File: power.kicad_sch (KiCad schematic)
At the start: 63 parts, among them U605 TPS566231P, U606 TPS566231P, U607 TPS566231P, U608 TPS566231P

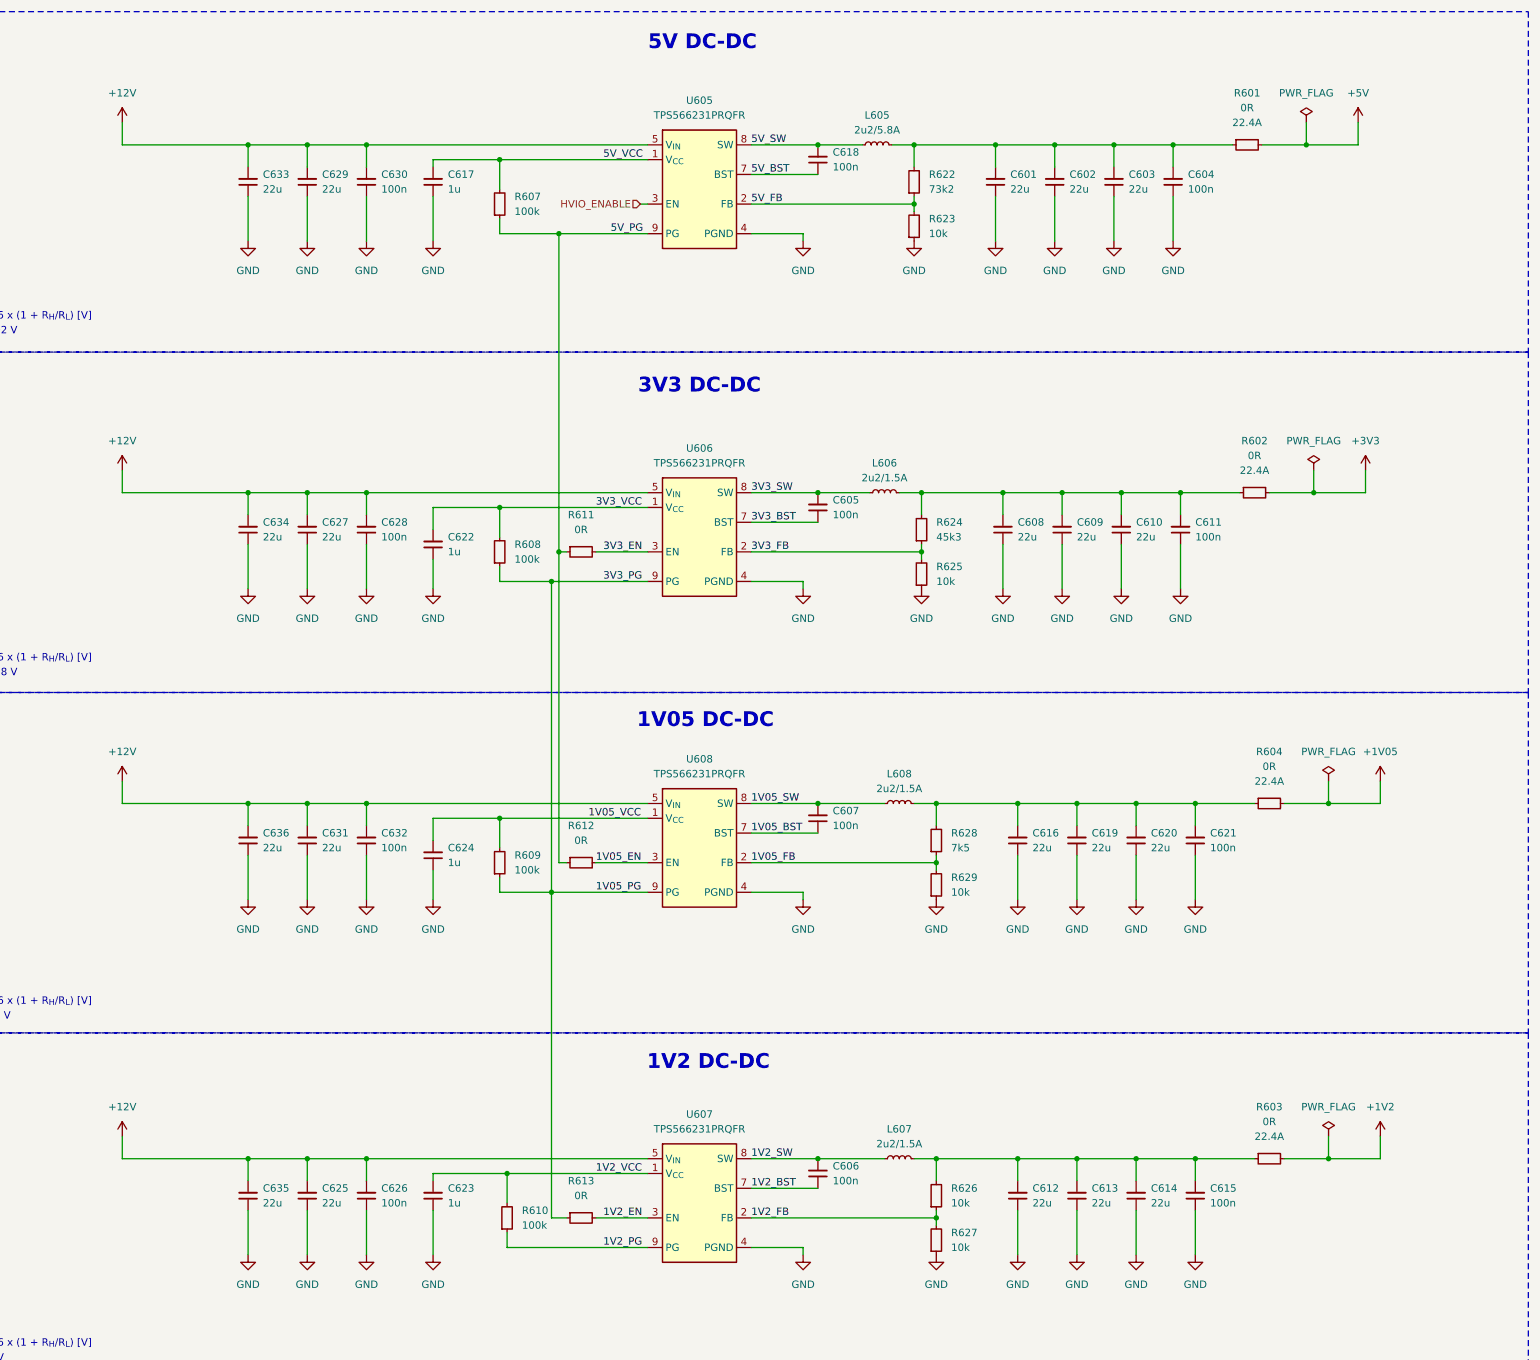
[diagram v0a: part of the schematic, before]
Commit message: [#99974] Import DC-SCM ports on root schematic, start connecting them to other blocks
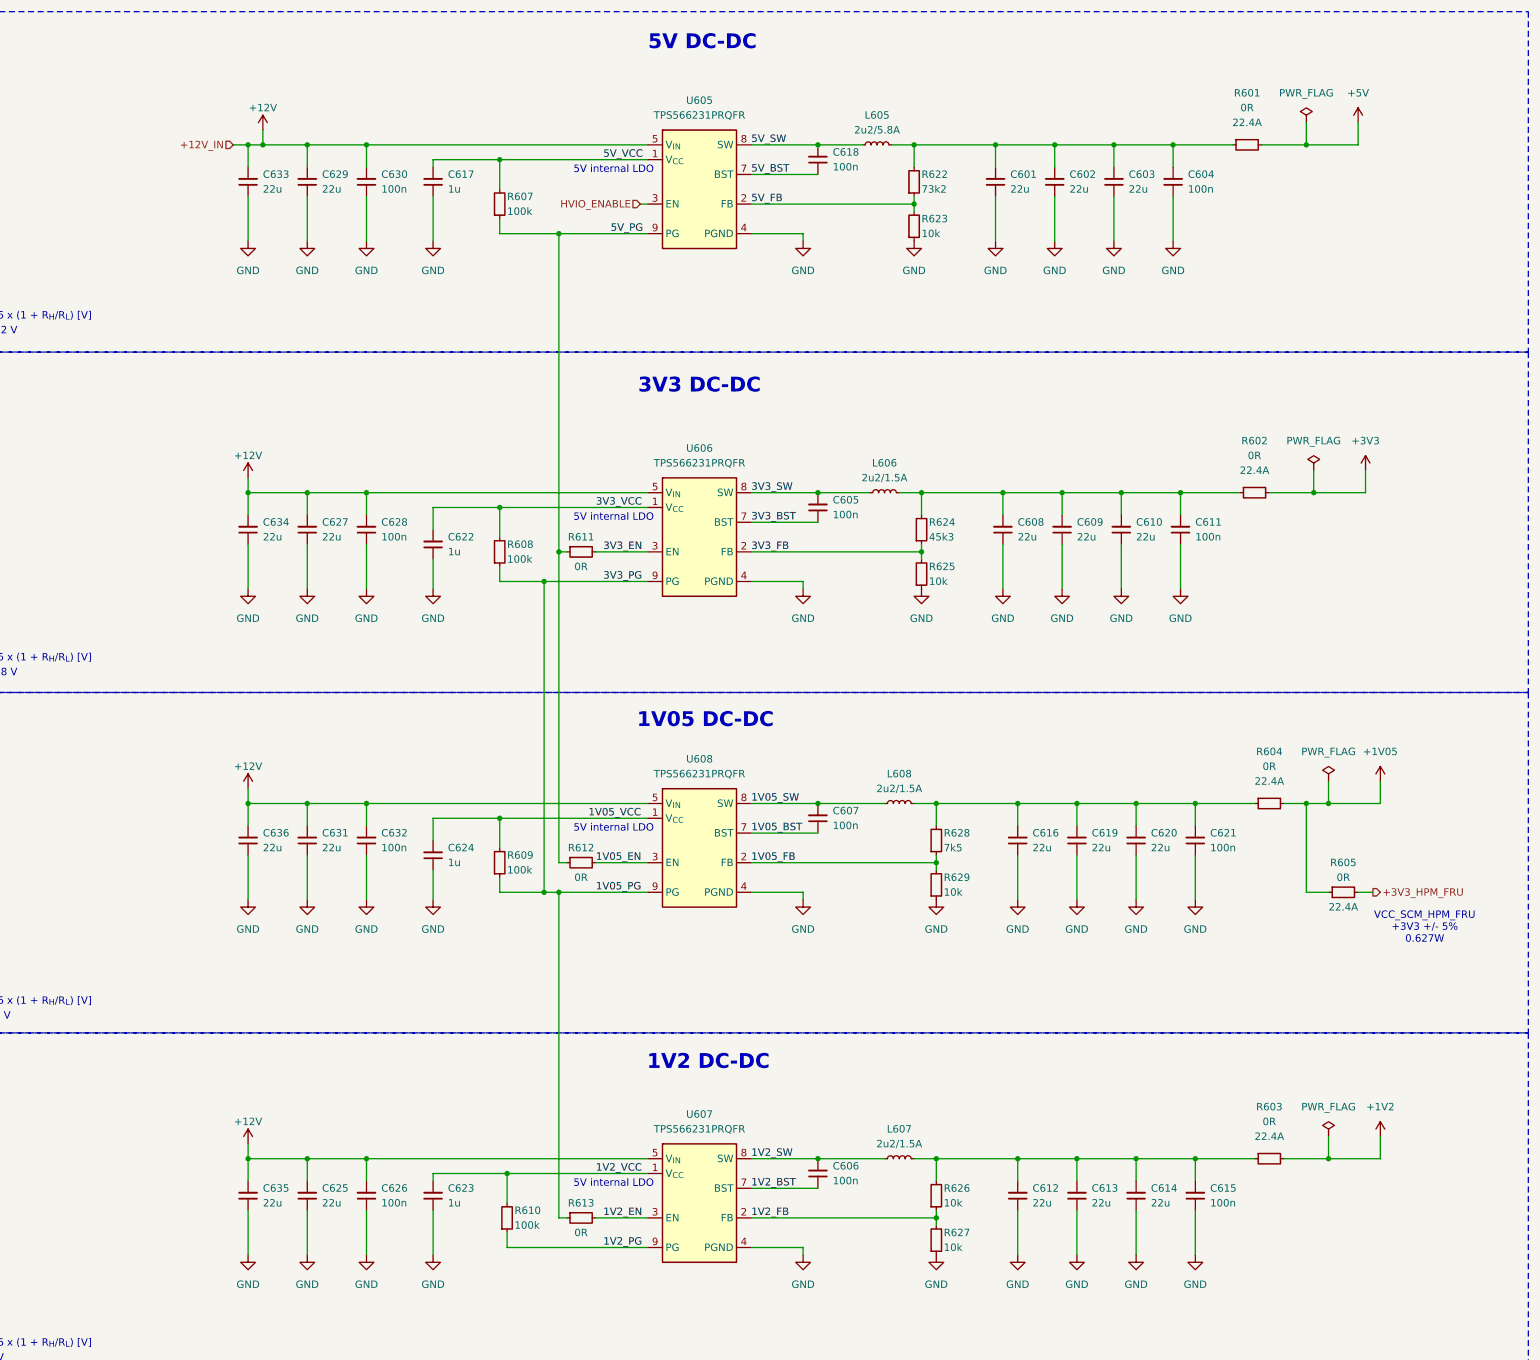
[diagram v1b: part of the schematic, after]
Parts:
- added R605: R_0R_22.4A_0603, antmicro-footprints:R_0603_1608Metric, symbol antmicroResistors0603:R_0R_22.4A_0603
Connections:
- net +1V05: now also R605.1
- new net +3V3_HPM_FRU: R605.2
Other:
- note added: "5V internal LDO"
- note added: "VCC_SCM_HPM_FRU +3V3 +/- 5% 0.627W"

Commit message: [#99649] Fix HS connector rule area, add DP AUX, HPD and CONFIG pins to DP bus, connect most signals on root schematic
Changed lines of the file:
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@@
 		(company "Altera")
-	)
-	(rectangle
-		(start 72.39 193.04)
-		(end 347.98 251.46)
-		(stroke
-			(width 0)
-			(type dash)
-			(color 7 57 255 1)
-		)
-		(fill
-			(type none)
-		)
-	)
-	(rectangle
-		(start 72.39 17.78)
-		(end 347.98 76.2)
-		(stroke
-			(width 0)
-			(type dash)
-			(color 7 57 255 1)
-		)
-		(fill
-			(type none)
-		)
-	)
-	(rectangle
-		(start 72.39 134.62)
-		(end 347.98 193.04)
-		(stroke
-			(width 0)
-			(type dash)
-			(color 7 57 255 1)
-		)
-		(fill
-			(type none)
-		)
-	)
-	(rectangle
-		(start 72.39 76.2)
-		(end 347.98 134.62)
-		(stroke
-			(width 0)
-			(type dash)
-			(color 7 57 255 1)
-		)
-		(fill
-			(type none)
-		)
 	)
 	(text "-->"
@@
 		)
 	)
+	(polyline
+		(pts
+			(xy 12.7 134.62) (xy 407.67 134.62)
+		)
+		(stroke
+			(width 0)
+			(type dash)
+		)
+	)
 	(wire
 		(pts
@@
 		)
 	)
+	(polyline
+		(pts
+			(xy 12.7 193.04) (xy 407.67 193.04)
+		)
+		(stroke
+			(width 0)
+			(type dash)
+		)
+	)
 	(wire
 		(pts
@@
 		)
 	)
+	(polyline
+		(pts
+			(xy 12.7 76.2) (xy 407.67 76.2)
+		)
+		(stroke
+			(width 0)
+			(type dash)
+		)
+	)
 	(wire
 		(pts
@@
 		)
 	)
+	(polyline
+		(pts
+			(xy 12.7 252.73) (xy 407.67 252.73)
+		)
+		(stroke
+			(width 0)
+			(type dash)
+		)
+	)

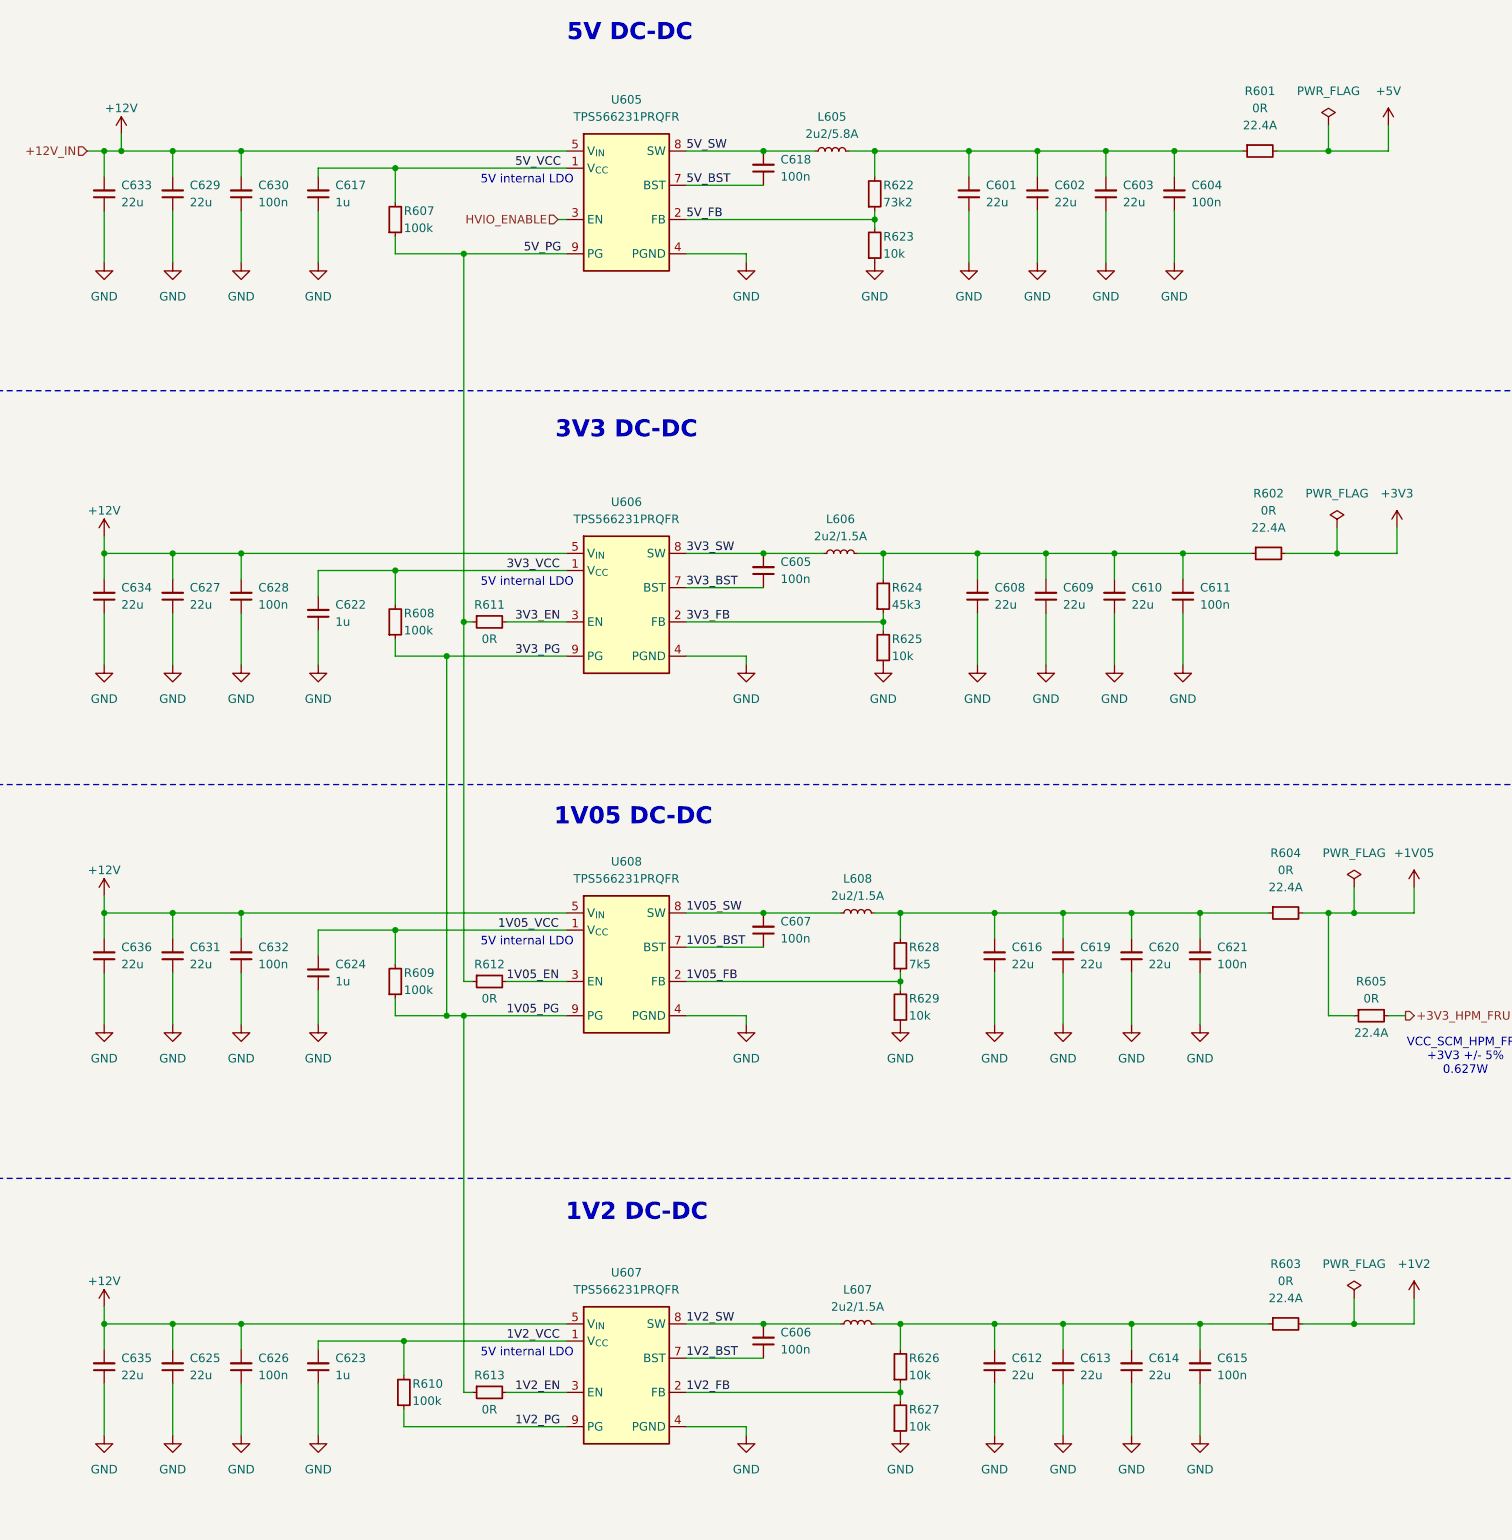
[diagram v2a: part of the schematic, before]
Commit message: [#100282] Reorder schematic pages, reannotate schematic
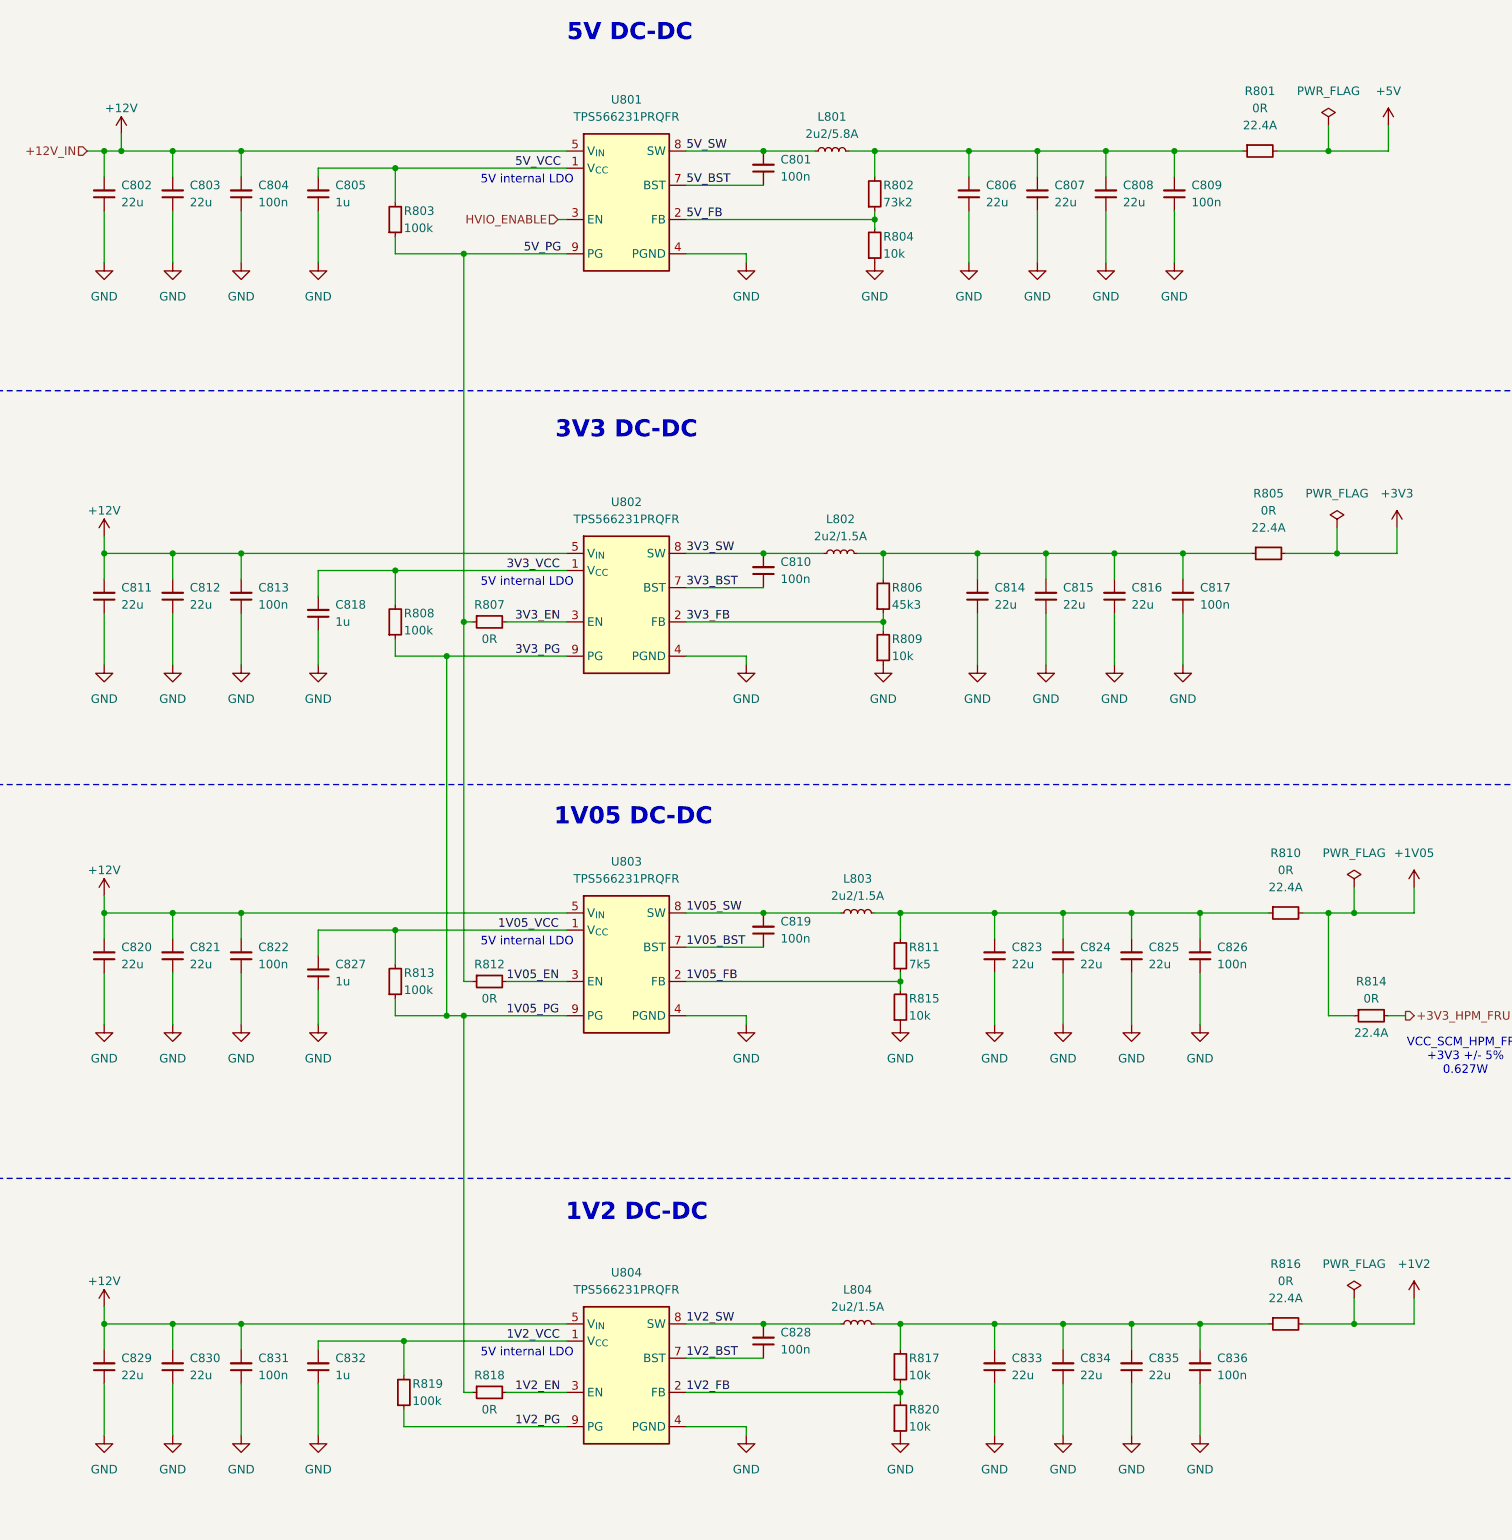
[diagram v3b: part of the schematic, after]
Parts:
- renumbered C618 to C801, C633 to C802, C629 to C803, C630 to C804, C617 to C805, C601 to C806, C602 to C807, C603 to C808, C604 to C809, C605 to C810, C634 to C811, C627 to C812, C628 to C813, C608 to C814, C609 to C815, C610 to C816, C611 to C817, C622 to C818, C607 to C819, C636 to C820, C631 to C821, C632 to C822, C616 to C823, C619 to C824, C620 to C825, C621 to C826, C624 to C827, C606 to C828, C635 to C829, C625 to C830, C626 to C831, C623 to C832, C612 to C833, C613 to C834, C614 to C835, C615 to C836, L605 to L801, L606 to L802, L608 to L803, L607 to L804, R601 to R801, R622 to R802, R607 to R803, R623 to R804, R602 to R805, R624 to R806, R611 to R807, R608 to R808, R625 to R809, R604 to R810, R628 to R811, R612 to R812, R609 to R813, R605 to R814, R629 to R815, R603 to R816, R626 to R817, R613 to R818, R610 to R819, R627 to R820, U605 to U801, U606 to U802, U608 to U803, U607 to U804
